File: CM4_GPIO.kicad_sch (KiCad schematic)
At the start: 33 parts, among them J12 Conn_02x07_Odd_Even, J13 Conn_01x03, J14 Conn_01x03, J15 Audio OUT, J16 Micro_SD_Card_Det, J17 THD-20-R, U10 74LVC1G07SE-7, U11 RT9742GGJ5, U8 74LVC1G07SE-7, U9 NC7WZ16

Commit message: Removing U1
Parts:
- removed J12: Conn_02x07_Odd_Even, Connector_PinHeader_2.54mm:PinHeader_2x07_P2.54mm_Vertical, symbol Connector_Generic:Conn_02x07_Odd_Even

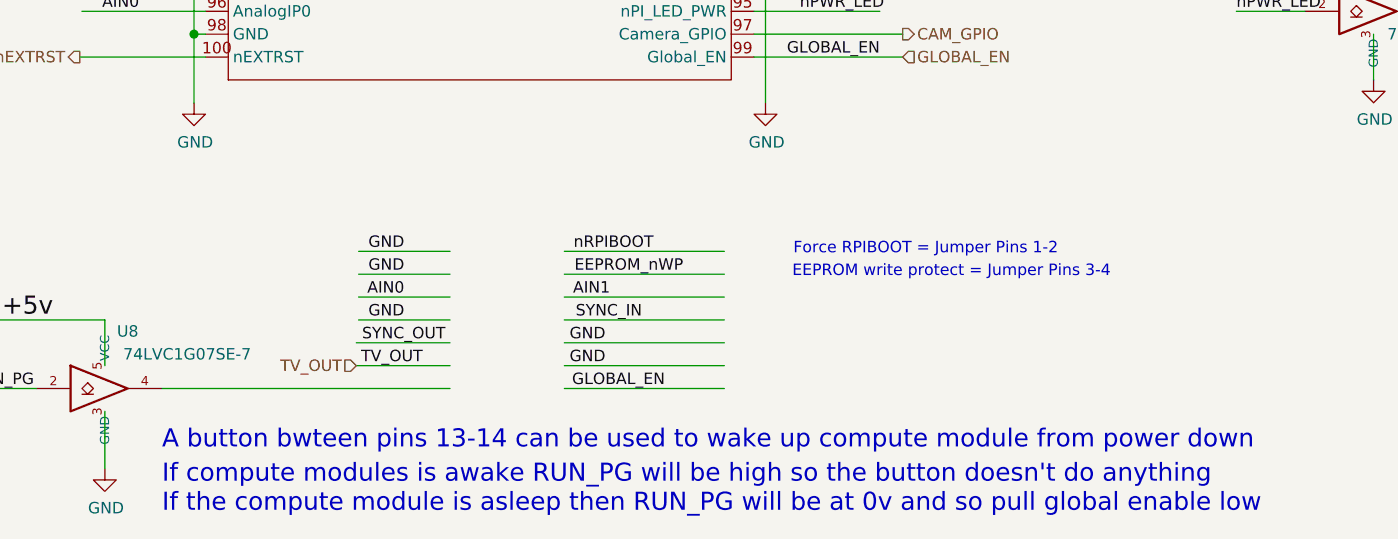
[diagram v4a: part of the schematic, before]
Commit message: Adding GlobalENable, and RpiBoot
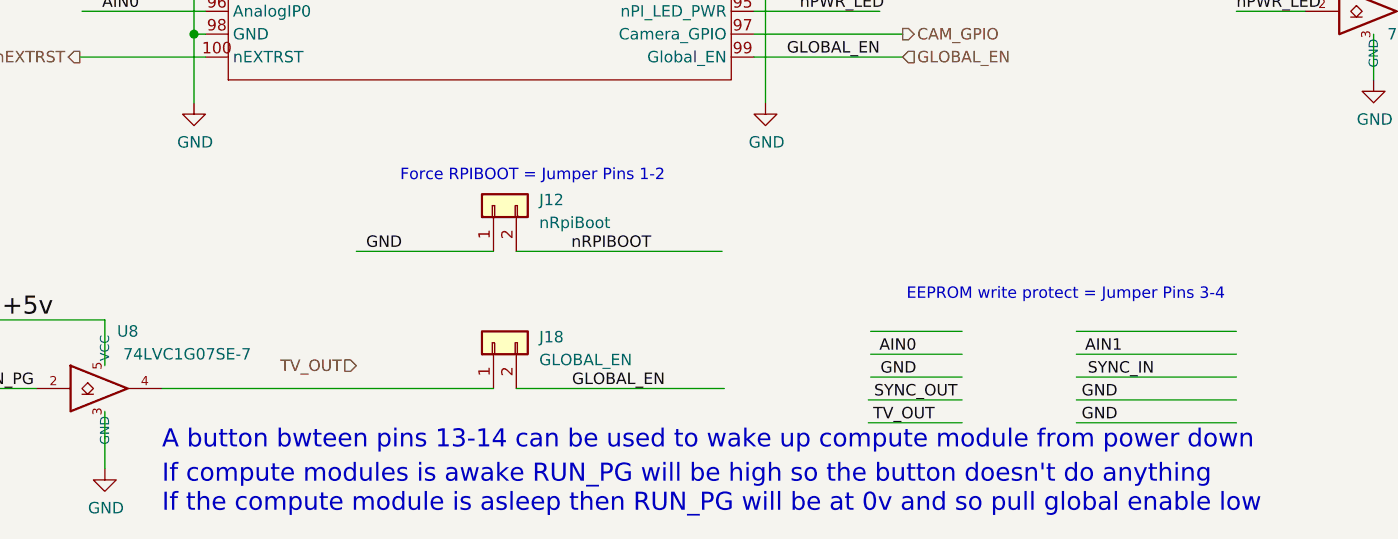
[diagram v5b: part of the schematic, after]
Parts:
- added J12: nRpiBoot, symbol Connector_Generic:Conn_01x02
- added J18: GLOBAL_EN, symbol Connector_Generic:Conn_01x02
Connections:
- net GLOBAL_EN: now also J18.2 (Pin_2)
- net GND: now also J12.1 (Pin_1)
- net nRPIBOOT: now also J12.2 (Pin_2)
- net at U8.4: now also J18.1 (Pin_1)

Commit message: Adding audio connector - fixing USB, adding logos
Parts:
- removed J15: Audio OUT, Connector_Audio:Jack_3.5mm_PJ311_Horizontal, symbol CM4IO:AudioJack3_Ground
- added U (x2): (no value), symbol Device:FerriteBead_Small
- added U: (no value), symbol Device:C
- added U: (no value), symbol Connector_Generic:Conn_01x03
- added U: (no value), symbol CM4IO:AudioJack3_Ground_SwitchTR
- U: renamed from U10; value 74LVC1G07SE-7 -> (none); footprint Package_TO_SOT_SMD:SOT-353_SC-70-5 -> (none)
- U: renamed from U8; value 74LVC1G07SE-7 -> (none); footprint Package_TO_SOT_SMD:SOT-353_SC-70-5 -> (none)
- U: renamed from U11; value RT9742GGJ5 -> (none); footprint Package_TO_SOT_SMD:SOT-23-5 -> (none)
- U: renamed from Module1; value ComputeModule4 -> (none); footprint CM4IO:Raspberry-Pi-4-Compute-Module-noholes -> (none)
- U: renamed from J17; value THD-20-R -> (none); footprint Connector_PinHeader_2.54mm:PinHeader_2x20_P2.54mm_Vertical -> (none)
- U: renamed from C40; value 10u -> (none); footprint Capacitor_SMD:C_0805_2012Metric -> (none)
- U: renamed from D3; value LED Green -> (none); footprint LED_SMD:LED_0603_1608Metric -> (none)
- U: renamed from R20; value 1k -> (none); footprint Resistor_SMD:R_0402_1005Metric -> (none)
- U: renamed from D4; value LED Red -> (none); footprint LED_SMD:LED_0603_1608Metric -> (none)
- U: renamed from R23; value 1k -> (none); footprint Resistor_SMD:R_0402_1005Metric -> (none)
- U: renamed from J14; value Conn_01x03 -> (none); footprint Connector_PinHeader_2.54mm:PinHeader_1x03_P2.54mm_Vertical -> (none)
- U: renamed from R30; value 0R -> (none); footprint Resistor_SMD:R_0805_2012Metric_Pad1.20x1.40mm_HandSolder -> (none)
- U: renamed from R31; value nf -> (none); footprint Resistor_SMD:R_0805_2012Metric_Pad1.20x1.40mm_HandSolder -> (none)
- U: renamed from J16; value Micro_SD_Card_Det -> (none); footprint CM4IO:SDCARD_MOLEX_503398-1892 -> (none)
- U: renamed from J13; value Conn_01x03 -> (none); footprint Connector_PinHeader_2.54mm:PinHeader_1x03_P2.54mm_Vertical -> (none)
- U: renamed from C38; value 47u 6.3 -> (none); footprint Capacitor_SMD:C_0805_2012Metric -> (none)
- U: renamed from R26; value 1K8 -> (none); footprint Resistor_SMD:R_0402_1005Metric -> (none)
- U: renamed from C39; value 47u 6.3 -> (none); footprint Capacitor_SMD:C_0805_2012Metric -> (none)
- U: renamed from R21; value 220 -> (none); footprint Resistor_SMD:R_0402_1005Metric -> (none)
- U: renamed from C36; value 100n 6.3 -> (none); footprint Capacitor_SMD:C_0402_1005Metric -> (none)
- U: renamed from R22; value 220 -> (none); footprint Resistor_SMD:R_0402_1005Metric -> (none)
- U: renamed from C35; value 100n 6.3 -> (none); footprint Capacitor_SMD:C_0402_1005Metric -> (none)
- U: renamed from C37; value 100n 6.3 -> (none); footprint Capacitor_SMD:C_0402_1005Metric -> (none)
- U: renamed from R28; value nf -> (none); footprint Resistor_SMD:R_0402_1005Metric -> (none)
- U: renamed from U9; value NC7WZ16 -> (none); footprint CM4IO:SC-88-6_2x2.1mm -> (none)
- U: renamed from J12; value nRpiBoot -> (none)
- U: renamed from R32; value 12K 1% -> (none); footprint Resistor_SMD:R_0402_1005Metric -> (none)
- U: renamed from R29; value nf -> (none); footprint Resistor_SMD:R_0402_1005Metric -> (none)
- U: renamed from J18; value GLOBAL_EN -> (none)
- U: renamed from R25; value 100 -> (none); footprint Resistor_SMD:R_0402_1005Metric -> (none)
- U: renamed from R27; value 1K8 -> (none); footprint Resistor_SMD:R_0402_1005Metric -> (none)
- U: renamed from R24; value 100 -> (none); footprint Resistor_SMD:R_0402_1005Metric -> (none)
- U: renamed from D5; value BAV99 -> (none); footprint Package_TO_SOT_SMD:SOT-23 -> (none)
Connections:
- net +3.3v: now also U.1; no longer U.1, U.2 (A), U.5 (Vcc)
- net AUDIO_L: now also U.3
- net AUDIO_R: now also U.4
- net GND: now also U.2; no longer U.1, U.1, U.1, U.1, U.1 (K), U.2, U.2, U.2, U.2 (GND)
- net at U.3 (K): now also U.1
- new net: U.1, U.1, U.1, U.1, U.1, U.1 (K), U.2, U.2, U.2, U.2, U.2, U.2 (GND), U.2 (Pin_2)
- new net: U.1, U.1, U.2, U.2 (A), U.5 (Vcc)
- new net: U.1 (Pin_1), U.6
- new net: U.3 (Pin_3), U.5
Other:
- moved on the sheet: U
